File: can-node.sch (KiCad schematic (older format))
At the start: 0 parts

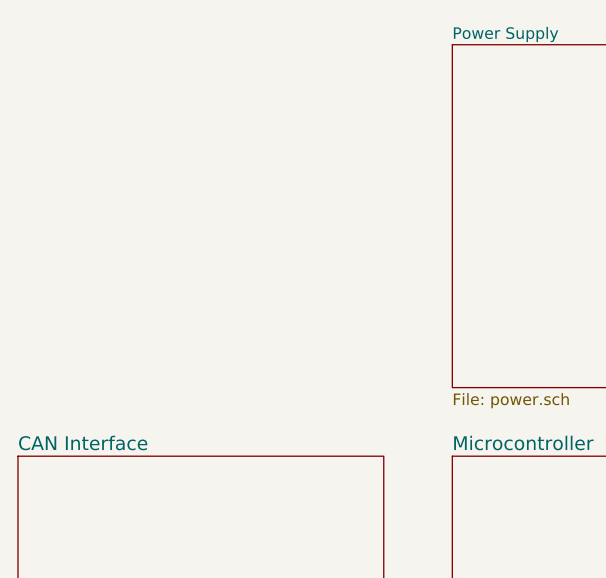
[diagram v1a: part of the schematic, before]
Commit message: Basic schematic with temparature and humidity sensor.
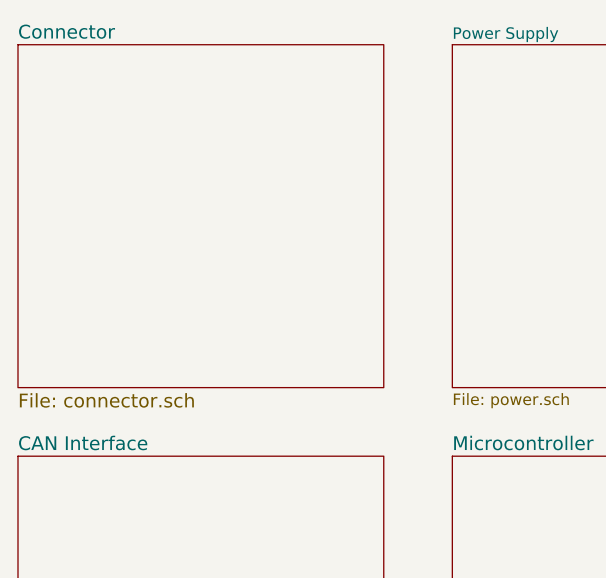
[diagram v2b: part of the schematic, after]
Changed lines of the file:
@@
 LIBS:74xx
 LIBS:74xgxx
+LIBS:can-node
 LIBS:can-node-cache
 EELAYER 25 0
@@
 $Descr A4 11693 8268
 encoding utf-8
-Sheet 1 4
+Sheet 1 5
 Title ""
 Date ""
@@
 F1 "can.sch" 60
 $EndSheet
+$Sheet
+S 1900 1300 1600 1500
+U 57AF4672
+F0 "Connector" 60
+F1 "connector.sch" 60
+$EndSheet
 $EndSCHEMATC

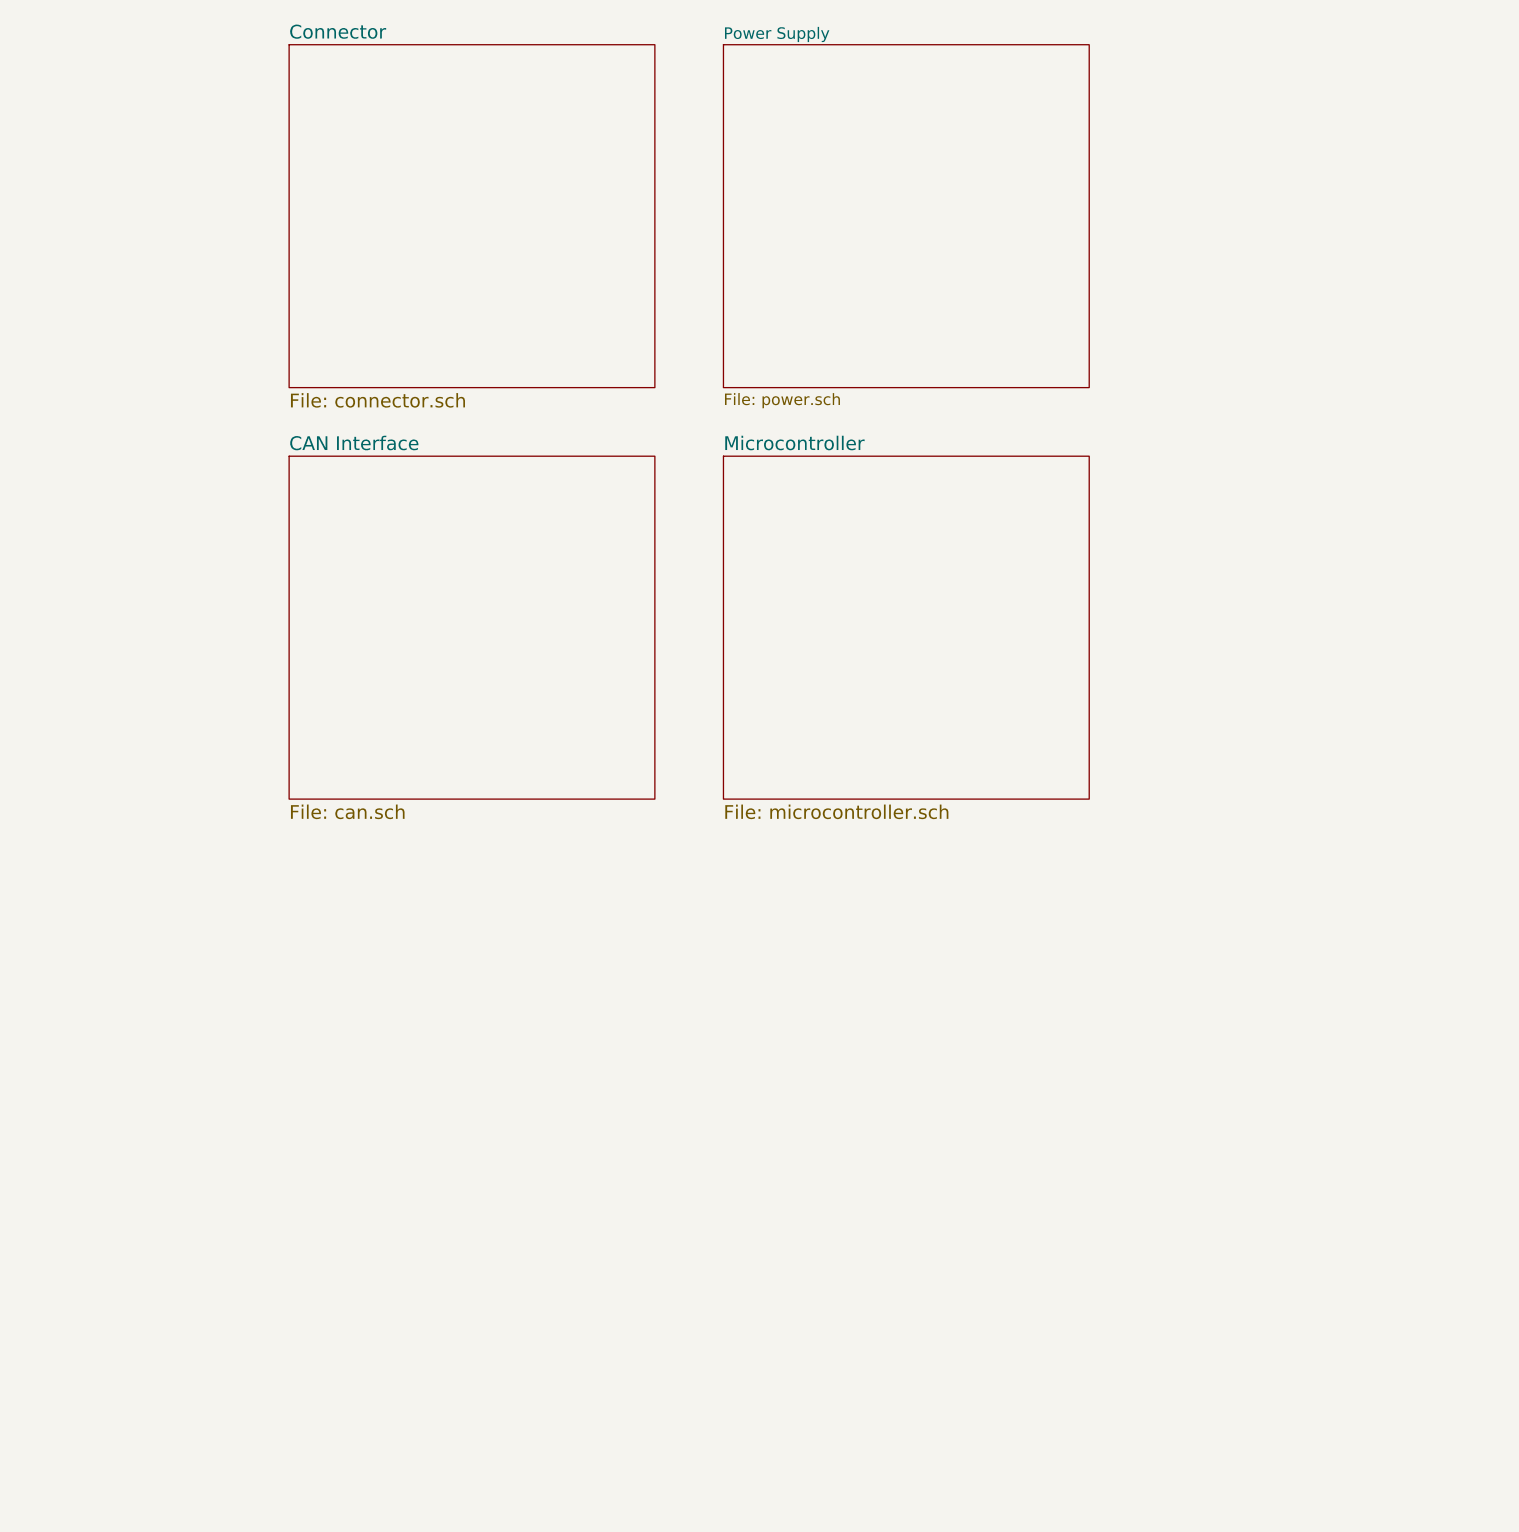
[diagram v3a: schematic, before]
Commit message: Some modifications to schematic, BOM, start releayout
- add LED display
- change crystal for RTC
- use components that are available at some distributors
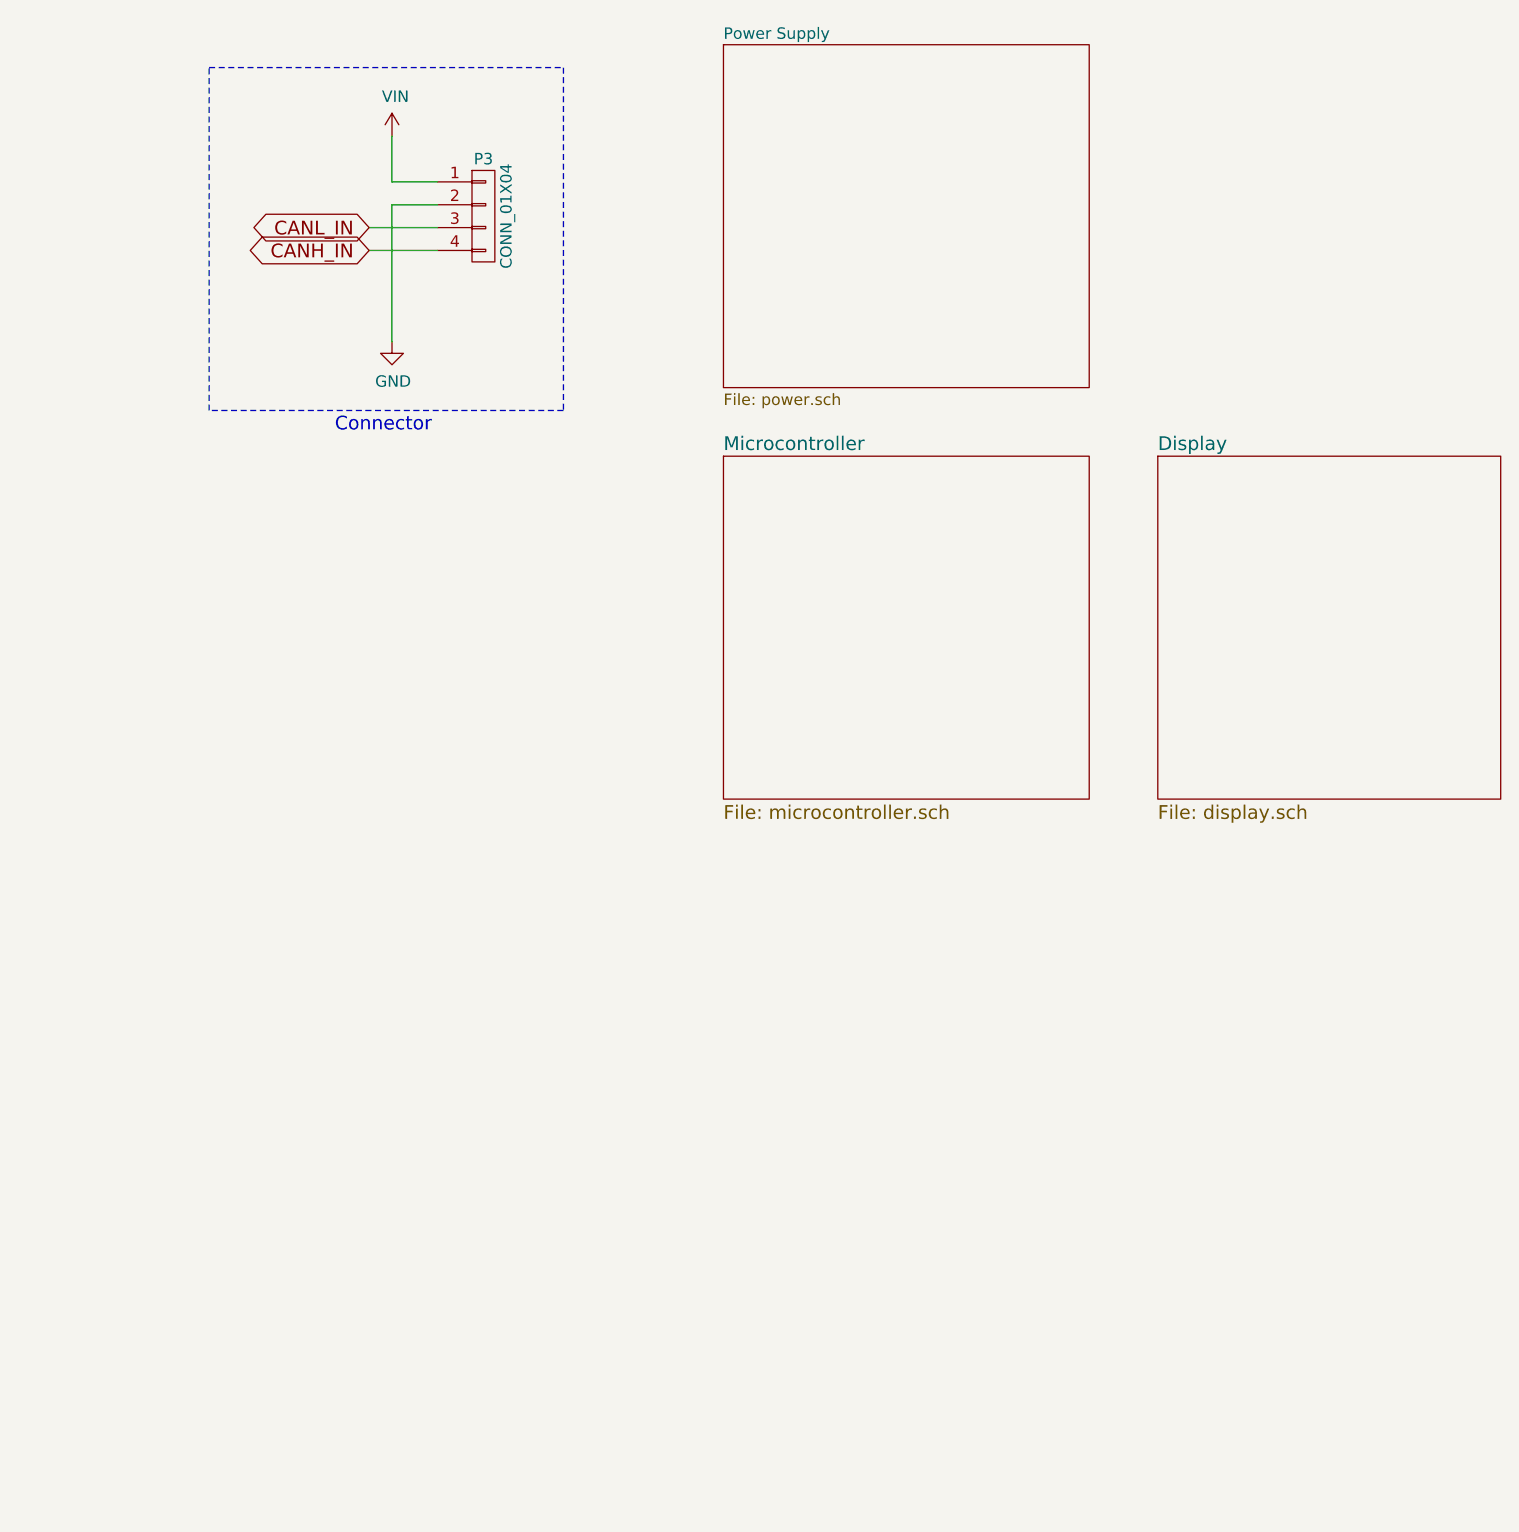
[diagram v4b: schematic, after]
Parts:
- added P3: CONN_01X04, can-node:WAGO_218-104, symbol CONN_01X04
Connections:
- new net CANH_IN: P3.4 (P4)
- new net CANL_IN: P3.3 (P3)
- new net GND: P3.2 (P2)
- new net VIN: P3.1 (P1)
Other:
- note added: "Connector"
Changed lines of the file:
@@
 $Descr A4 11693 8268
 encoding utf-8
-Sheet 1 5
+Sheet 1 4
 Title ""
 Date ""
@@
 F1 "microcontroller.sch" 60
 $EndSheet
+$Comp
+L GND #PWR01
+U 1 1 586A5601
+P 2350 2600
+F 0 "#PWR01" H 2350 2350 50  0001 C CNN
+F 1 "GND" H 2355 2427 50  0000 C CNN
+F 2 "" H 2350 2600 50  0000 C CNN
+F 3 "" H 2350 2600 50  0000 C CNN
+	1    2350 2600
+	1    0    0    -1
+$EndComp
+Text GLabel 2250 2100 0    60   BiDi ~ 0
+CANL_IN
+Text GLabel 2250 2200 0    60   BiDi ~ 0
+CANH_IN
+$Comp
+L VIN #PWR02
+U 1 1 586A5609
+P 2350 1700
+F 0 "#PWR02" H 2350 1550 50  0001 C CNN
+F 1 "VIN" H 2365 1873 50  0000 C CNN
+F 2 "" H 2350 1700 60  0000 C CNN
+F 3 "" H 2350 1700 60  0000 C CNN
+	1    2350 1700
+	1    0    0    -1
+$EndComp
+Wire Wire Line
+	2250 2200 2550 2200
+Wire Wire Line
+	2350 2600 2350 2000
+Wire Wire Line
+	2350 2000 2550 2000
+Wire Wire Line
+	2550 1900 2350 1900
+Wire Wire Line
+	2350 1900 2350 1700
+Wire Wire Line
+	2250 2100 2550 2100
+$Comp
+L CONN_01X04 P3
+U 1 1 586A5615
+P 2750 2050
+F 0 "P3" H 2750 2300 50  0000 C CNN
+F 1 "CONN_01X04" V 2850 2050 50  0000 C CNN
+F 2 "can-node:WAGO_218-104" H 2750 2050 50  0001 C CNN
+F 3 "" H 2750 2050 50  0000 C CNN
+	1    2750 2050
+	1    0    0    -1
+$EndComp
+Wire Notes Line
+	1550 1400 3100 1400
+Wire Notes Line
+	3100 1400 3100 2900
+Wire Notes Line
+	3100 2900 1550 2900
+Wire Notes Line
+	1550 2900 1550 1400
+Text Notes 2100 3000 0    60   ~ 0
+Connector
 $Sheet
-S 1900 3100 1600 1500
-U 562B5164
-F0 "CAN Interface" 60
-F1 "can.sch" 60
-$EndSheet
-$Sheet
-S 1900 1300 1600 1500
-U 57AF4672
-F0 "Connector" 60
-F1 "connector.sch" 60
+S 5700 3100 1500 1500
+U 586C20B6
+F0 "Display" 60
+F1 "display.sch" 60
 $EndSheet
 $EndSCHEMATC

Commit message: Add 24V outputs.
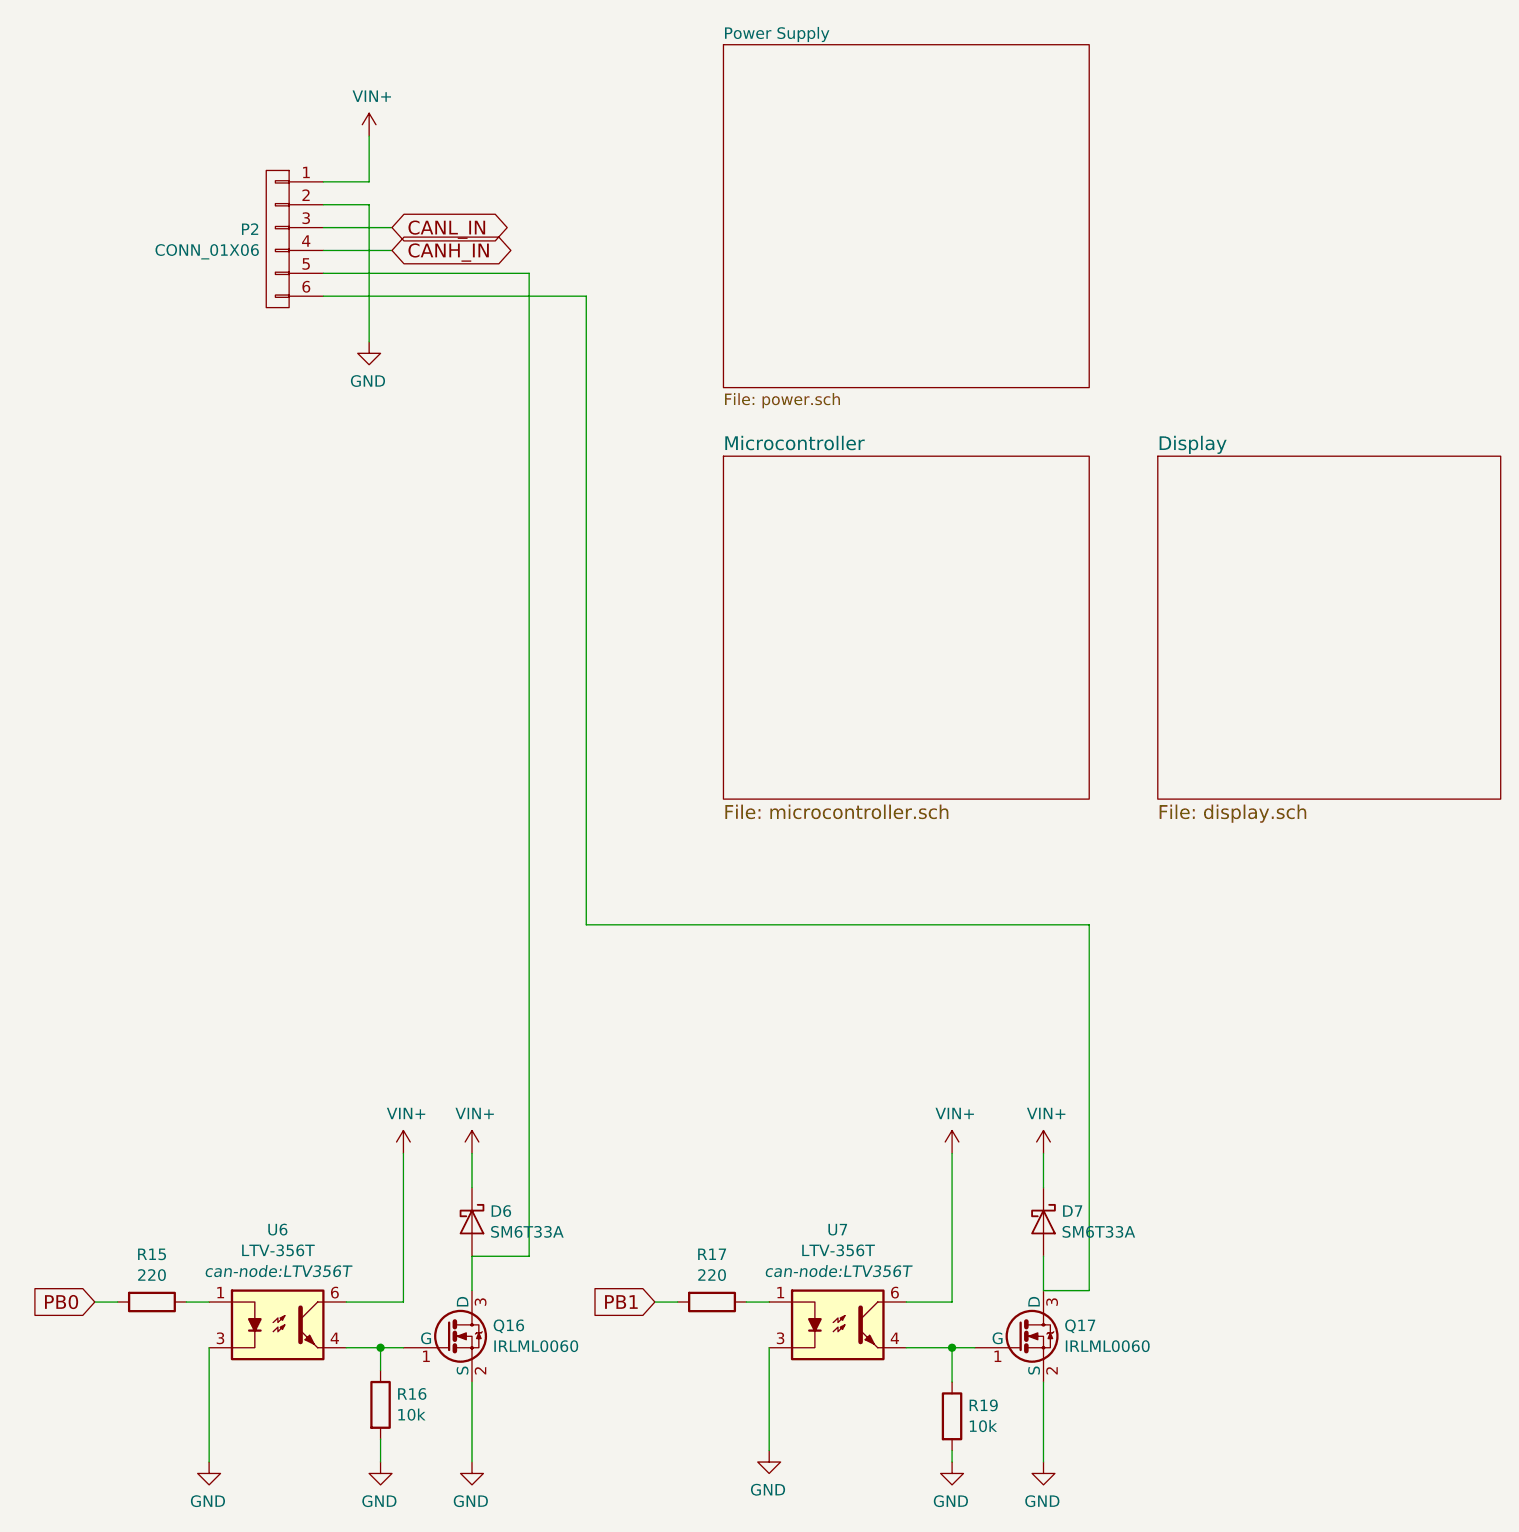
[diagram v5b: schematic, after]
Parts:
- removed P3: CONN_01X04, can-node:WAGO_218-104, symbol CONN_01X04
- added D6, D7: SM6T33A, Diodes_SMD:SMB_Standard, symbol D_Schottky
- added P2: CONN_01X06, can-node:WAGO_218-106, symbol CONN_01X06
- added Q16, Q17: IRLML0060, TO_SOT_Packages_SMD:SOT-23, symbol IRLML0060
- added R15, R17: 220, Resistors_SMD:R_0402, symbol R
- added R16, R19: 10k, Resistors_SMD:R_0402, symbol R
- added U6, U7: LTV-356T, can-node:LTV356T, symbol LTV-356T
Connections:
- net CANH_IN: now also P2.4 (P4)
- net CANL_IN: now also P2.3 (P3)
- net GND: now also P2.2 (P2), Q16.2 (S), Q17.2 (S), R16.2, R19.2, U6.3, U7.3
- new net: D6.2 (A), P2.5 (P5), Q16.3 (D)
- new net: D7.2 (A), P2.6 (P6), Q17.3 (D)
- new net: R17.1, U7.1
- new net: Q17.1 (G), R19.1, U7.4
- new net: R15.1, U6.1
- new net: Q16.1 (G), R16.1, U6.4
- new net PB0: R15.2
- new net PB1: R17.2
- new net VIN+: D6.1 (K), D7.1 (K), P2.1 (P1), U6.6, U7.6
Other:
- note removed: "Connector"
